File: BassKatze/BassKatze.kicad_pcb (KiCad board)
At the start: 2 copper layers, 16 parts, among them J1 USB_B_Micro, J2 Conn_01x02_Male, U1 ATmega328-AU, U2 MSGEQ7, U3 TP4056

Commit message: pcb wip
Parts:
- added Charge_Powerup1: D, Diode_THT:D_DO-15_P5.08mm_Vertical_KathodeUp, F.Cu at (73.0, 148.0)
- added D1: D, Diode_THT:D_DO-15_P2.54mm_Vertical_KathodeUp, F.Cu at (105.5, 112.9)
- added D10: SK6812, LED_SMD:LED_SK6812_PLCC4_5.0x5.0mm_P3.2mm, F.Cu at (116.8, 147.3)
- added D11: SK6812, LED_SMD:LED_SK6812_PLCC4_5.0x5.0mm_P3.2mm, F.Cu at (113.7, 141.0)
- added D12: SK6812, LED_SMD:LED_SK6812_PLCC4_5.0x5.0mm_P3.2mm, F.Cu at (111.8, 134.6)
- added D13: SK6812, LED_SMD:LED_SK6812_PLCC4_5.0x5.0mm_P3.2mm, F.Cu at (110.5, 128.3)
- added D14: SK6812, LED_SMD:LED_SK6812_PLCC4_5.0x5.0mm_P3.2mm, F.Cu at (110.5, 121.9)
- added D15: SK6812, LED_SMD:LED_SK6812_PLCC4_5.0x5.0mm_P3.2mm, F.Cu at (112.4, 115.6)
- added D16: SK6812, LED_SMD:LED_SK6812_PLCC4_5.0x5.0mm_P3.2mm, F.Cu at (113.7, 109.2)
- added D17: SK6812, LED_SMD:LED_SK6812_PLCC4_5.0x5.0mm_P3.2mm, F.Cu at (120.7, 106.0)
- added D2: SK6812, LED_SMD:LED_SK6812_PLCC4_5.0x5.0mm_P3.2mm, F.Cu at (137.2, 106.7)
- added D3: SK6812, LED_SMD:LED_SK6812_PLCC4_5.0x5.0mm_P3.2mm, F.Cu at (138.4, 113.7)
- added D4: SK6812, LED_SMD:LED_SK6812_PLCC4_5.0x5.0mm_P3.2mm, F.Cu at (144.8, 114.9)
- added D5: SK6812, LED_SMD:LED_SK6812_PLCC4_5.0x5.0mm_P3.2mm, F.Cu at (144.8, 121.9)
- added D6: SK6812, LED_SMD:LED_SK6812_PLCC4_5.0x5.0mm_P3.2mm, F.Cu at (144.8, 128.3)
- added D7: SK6812, LED_SMD:LED_SK6812_PLCC4_5.0x5.0mm_P3.2mm, F.Cu at (142.9, 134.6)
- added D8: SK6812, LED_SMD:LED_SK6812_PLCC4_5.0x5.0mm_P3.2mm, F.Cu at (140.3, 141.0)
- added D9: SK6812, LED_SMD:LED_SK6812_PLCC4_5.0x5.0mm_P3.2mm, F.Cu at (136.5, 147.3)
- added Q1: IRF7404, Package_SO:SOIC-8_3.9x4.9mm_P1.27mm, B.Cu at (146.8, 127.0)
- added R4: 250Ohm, Resistor_SMD:R_1206_3216Metric_Pad1.42x1.75mm_HandSolder, B.Cu at (141.6, 122.7)
- added R5: 10KOhm, Resistor_SMD:R_1206_3216Metric_Pad1.42x1.75mm_HandSolder, B.Cu at (137.2, 104.8)
- added SW1: SW_Push, Capacitor_SMD:C_1210_3225Metric, B.Cu at (145.7, 132.1)
- C1, C2, C3, C4, C5, C6, R1, R2, R3, RProg1, U1: moved to B.Cu
- J1: value USB_B_Micro -> Conn_01x02_Female; footprint Connector_PinHeader_2.54mm:PinHeader_1x06_P2.54mm_Vertical -> Capacitor_SMD:C_1210_3225Metric; moved to B.Cu
- J2: footprint Connector_JST:JST_EH_B2B-EH-A_1x02_P2.50mm_Vertical -> Capacitor_SMD:C_1210_3225Metric; moved to B.Cu
- U3: footprint Package_SO:HSOP-8-1EP_3.9x4.9mm_P1.27mm_EP2.41x3.1mm_ThermalVias -> tp4056:TP4056_SOP-8-PP; moved to B.Cu
- moved C4 93.0 mm to (119.1, 150.0), turned to 180 degrees
- moved U2 92.7 mm to (130.8, 149.9), turned to 180 degrees
- moved C6 90.5 mm to (119.3, 144.8), turned to 180 degrees
- moved R3 88.2 mm to (127.0, 152.9)
- moved C5 79.7 mm to (134.9, 149.9)
- moved C3 66.1 mm to (132.5, 139.4)
- moved R2 65.5 mm to (137.7, 139.4)
- moved J2 64.6 mm to (151.3, 133.2), turned to 90 degrees
- moved U3 57.4 mm to (145.3, 115.1)
- moved J1 56.5 mm to (127.1, 113.9)
- moved U1 56.4 mm to (116.8, 110.5)
- moved R1 53.2 mm to (132.5, 114.0)
- moved C2 53.0 mm to (151.5, 121.4), turned to 90 degrees
- moved C1 46.0 mm to (145.3, 119.5), turned to 180 degrees
- moved RProg1 45.0 mm to (138.6, 116.8), turned to 270 degrees
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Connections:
- ISP1 pad 2: SCK -> (no net)
- ISP1 pad 3: Reset -> SCK
- ISP1 pad 4: BAT- -> MOSI
- ISP1 pad 5: MOSI -> Reset
- ISP1 pad 6: (no net) -> BAT-
- J1 pad 1: 5V_IN -> BAT-
- J1 pad 2: (no net) -> 5V_IN
- U1 pad 11: (no net) -> STDBY
- U1 pad 2: (no net) -> Button
- U1 pad 32: (no net) -> LED1
- U1 pad 9: (no net) -> PWR_HOLD
- U3 pad 6: (no net) -> STDBY
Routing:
- net BAT-: track 0.00 -> 263.0 mm, vias 0 -> 8
- net PWR: track 0.00 -> 169.2 mm, vias 0 -> 4
- net RAW_Spectrum: track 0.00 -> 51.2 mm, vias 0 -> 3
- net EQ_Band: track 0.00 -> 44.3 mm
- net EQ_Reset: track 0.00 -> 44.1 mm
- net LED1: track 0.00 -> 30.0 mm, vias 0 -> 3
- net Reset: track 0.00 -> 29.1 mm
- net Net-(D10-Pad2): track 0.00 -> 25.1 mm
- net BAT+: track 0.00 -> 24.2 mm
- net MOSI: track 0.00 -> 13.8 mm
- net Net-(C1-Pad1): track 0.00 -> 12.0 mm
- net Net-(D10-Pad4): track 0.00 -> 9.39 mm
- net Net-(D11-Pad4): track 0.00 -> 8.38 mm
- net Button: track 0.00 -> 8.28 mm
- net SCK: track 0.00 -> 8.12 mm
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
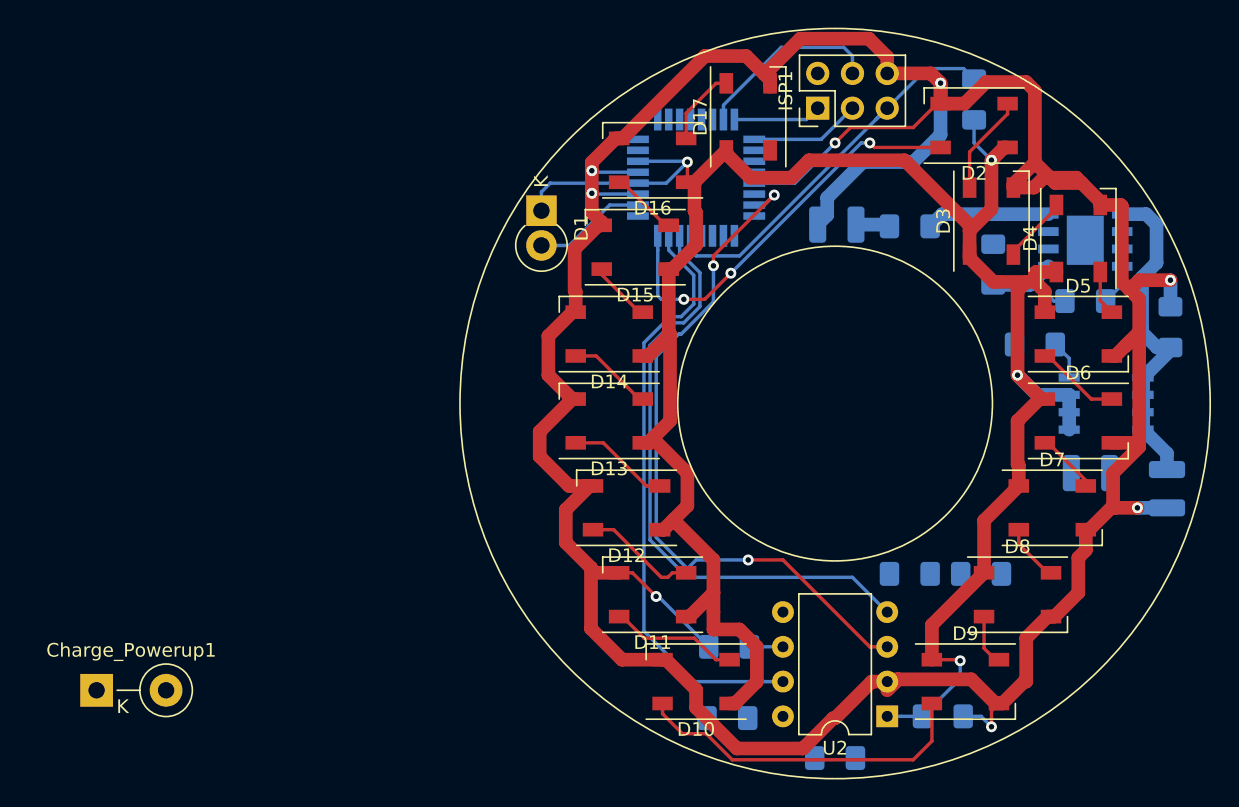
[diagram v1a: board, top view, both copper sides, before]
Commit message: with mic amplifier
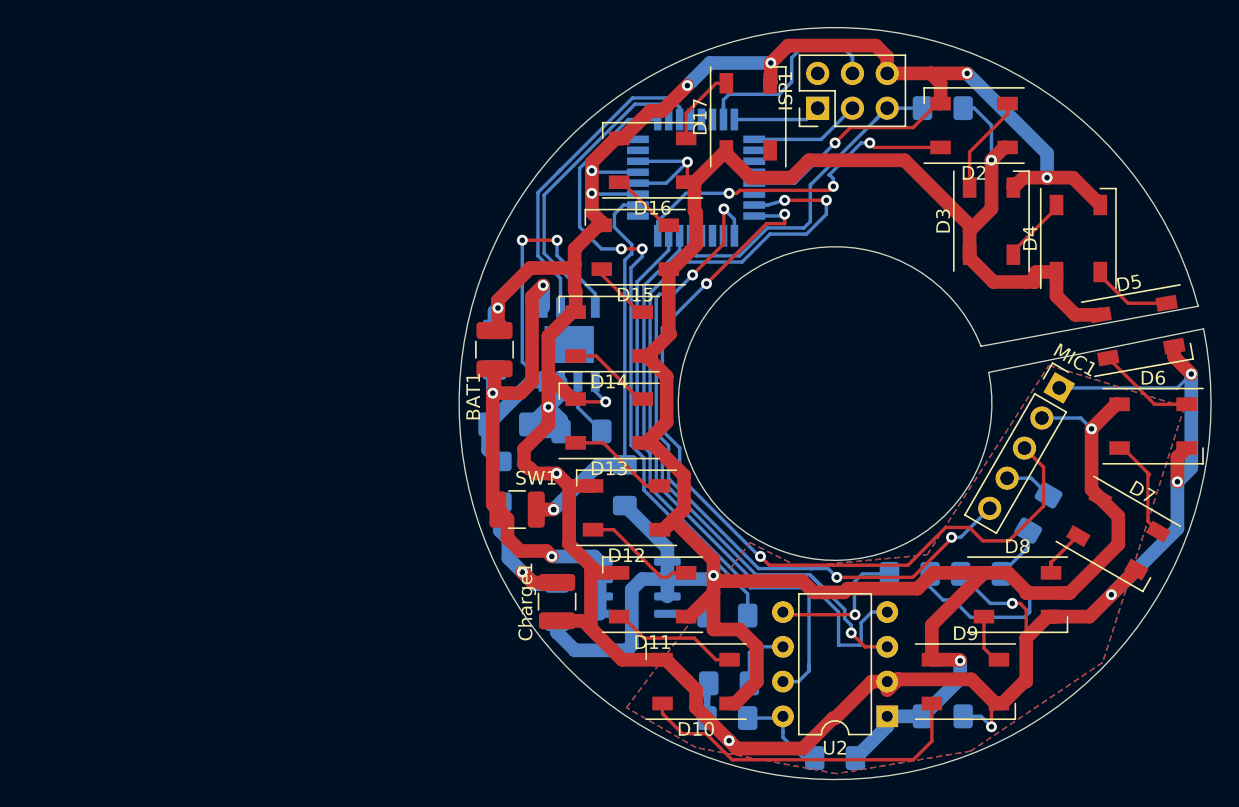
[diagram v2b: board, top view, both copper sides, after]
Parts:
- removed J1: Conn_01x02_Female, Capacitor_SMD:C_1210_3225Metric
- removed J2: Conn_01x02_Male, Capacitor_SMD:C_1210_3225Metric
- added BAT1: BAT, Capacitor_SMD:C_1210_3225Metric, F.Cu at (102.1, 123.1)
- added Charge1: Charge, Capacitor_SMD:C_1210_3225Metric, F.Cu at (106.7, 141.5)
- added MIC1: MIC, Connector_PinHeader_2.54mm:PinHeader_1x05_P2.54mm_Vertical, F.Cu at (143.4, 125.9)
- added R6: 147KOhm, Resistor_SMD:R_1206_3216Metric_Pad1.42x1.75mm_HandSolder, B.Cu at (141.9, 135.0)
- Charge_Powerup1: footprint Diode_THT:D_DO-15_P5.08mm_Vertical_KathodeUp -> Diode_SMD:D_1206_3216Metric; moved to B.Cu
- D1: footprint Diode_THT:D_DO-15_P2.54mm_Vertical_KathodeUp -> Diode_SMD:D_1206_3216Metric_Pad1.42x1.75mm_HandSolder; moved to B.Cu
- R2: value 22KOhm -> 26KOhm
- SW1: moved to F.Cu
- moved C2 49.4 mm to (102.1, 123.1)
- moved C1 43.1 mm to (103.1, 128.5), turned to 0 degrees
- moved SW1 42.0 mm to (103.8, 134.7), turned to 0 degrees
- moved U3 38.5 mm to (107.6, 122.7), turned to 90 degrees
- moved Q1 37.1 mm to (112.3, 140.5), turned to 180 degrees
- moved R1 35.3 mm to (102.5, 132.7), turned to 90 degrees
- moved Charge_Powerup1 34.2 mm to (106.7, 141.6), turned to 90 degrees
- moved RProg1 32.5 mm to (108.5, 129.0), turned to 180 degrees
- moved R4 30.0 mm to (119.1, 142.5), turned to 0 degrees
- moved D1 21.0 mm to (111.6, 133.0), turned to 90 degrees
- moved D6 5.47 mm to (150.2, 128.7)
- moved D7 5.19 mm to (147.7, 136.5), turned to 330 degrees
- moved D5 4.33 mm to (149.1, 121.7), turned to 10 degrees
- moved C6 2.67 mm to (119.3, 147.4)
- moved R5 2.37 mm to (134.9, 105.4), turned to 0 degrees
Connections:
- R2 pad 1: Net-(C3-Pad2) -> BAT-
- R2 pad 2: (no net) -> Net-(C3-Pad2)
- U1 pad 10: (no net) -> CHRG
- U1 pad 24: (no net) -> Gain_Select
- U1 pad 25: (no net) -> Attack_Select
- U3 pad 7: (no net) -> CHRG
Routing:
- net Gain_Select: track 0.00 -> 63.2 mm, vias 0 -> 3
- net Attack_Select: track 0.00 -> 53.7 mm, vias 0 -> 4
- net PWR_HOLD: track 0.00 -> 47.4 mm, vias 0 -> 2
- net PWR: track 169.2 -> 213.5 mm, vias 4 -> 5
- net STDBY: track 0.00 -> 23.8 mm
- net CHRG: track 0.00 -> 22.2 mm
- net Button: track 8.28 -> 30.4 mm, vias 0 -> 2
- net Net-(C3-Pad2): track 0.00 -> 17.7 mm
- net Net-(C1-Pad1): track 12.0 -> 28.4 mm, vias 0 -> 2
- net BAT+: track 24.2 -> 38.1 mm, vias 0 -> 3
- net Net-(C3-Pad1): track 0.00 -> 10.6 mm, vias 0 -> 1
- net RAW_Spectrum: track 51.2 -> 61.7 mm
- net 5V_IN: track 2.50 -> 11.6 mm, vias 0 -> 1
- net Net-(C4-Pad1): track 0.00 -> 7.12 mm
- net LED1: track 30.0 -> 25.2 mm
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- added copper zone on B.Cu, net BAT-
- added copper zone on F.Cu, net BAT-
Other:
- board outline added: 55 x 54.9 mm

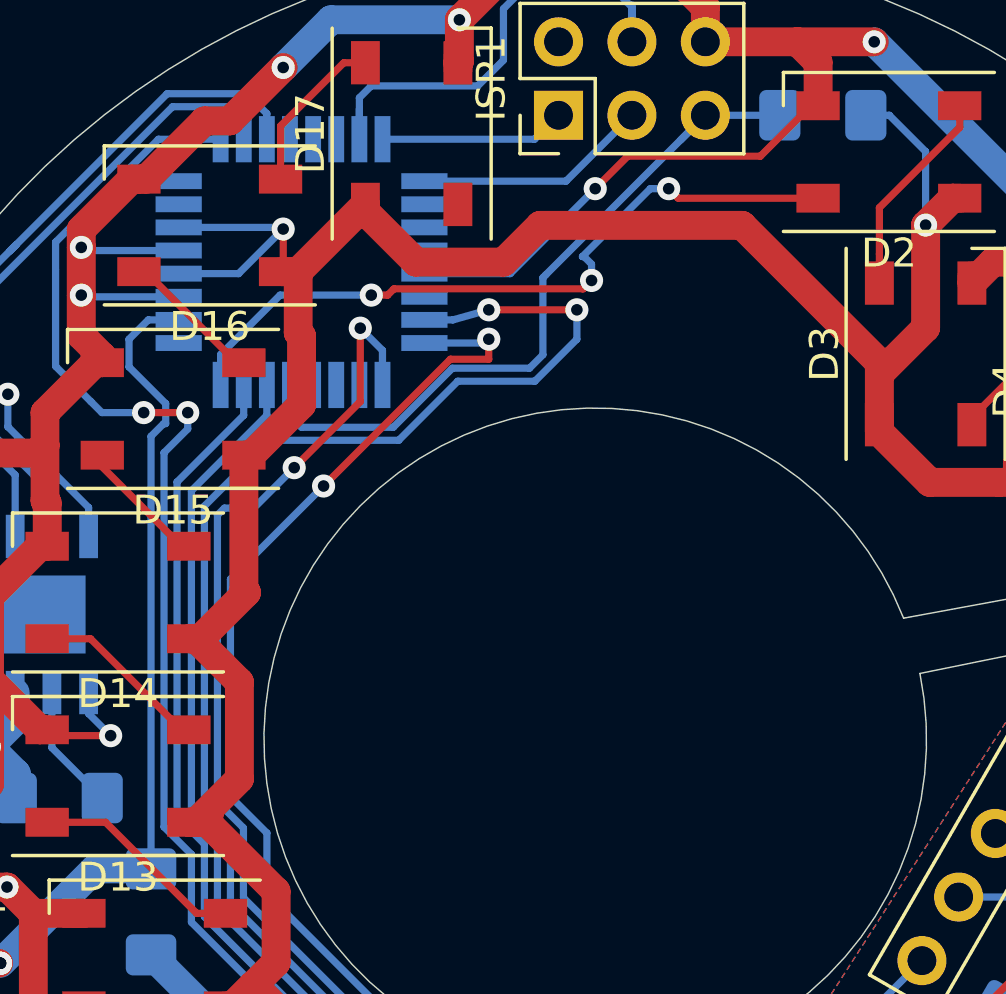
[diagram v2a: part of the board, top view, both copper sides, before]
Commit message: added rx/tx header for serial debugging started dummy application
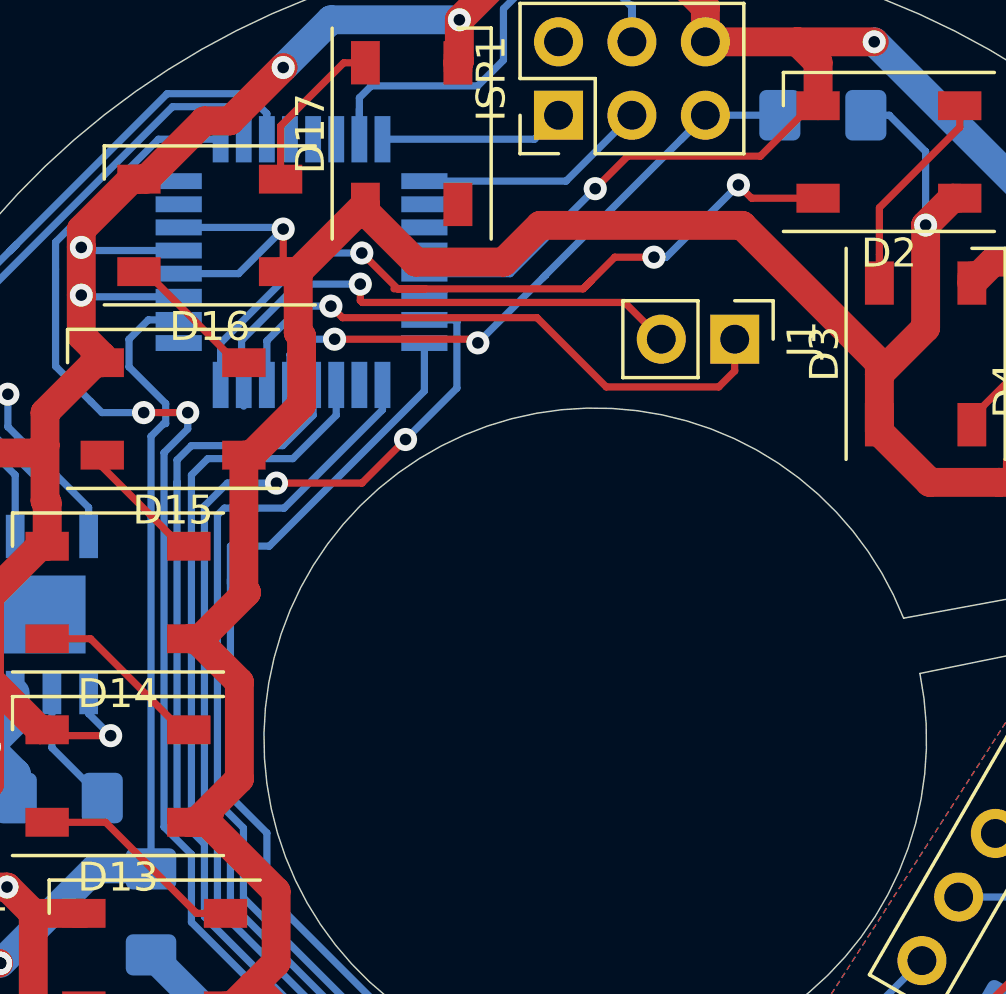
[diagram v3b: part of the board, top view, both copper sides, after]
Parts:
- added J1: Conn_01x02_Female, Connector_PinHeader_2.54mm:PinHeader_1x02_P2.54mm_Vertical, F.Cu at (131.8, 113.2)
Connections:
- U1 pad 27: (no net) -> EQ_Band
- U1 pad 28: (no net) -> EQ_Reset
- U1 pad 30: EQ_Band -> Net-(J1-Pad1)
- U1 pad 31: EQ_Reset -> Net-(J1-Pad2)
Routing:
- net Net-(J1-Pad1): track 0.00 -> 20.7 mm, vias 0 -> 1
- net Net-(J1-Pad2): track 0.00 -> 18.8 mm, vias 0 -> 1
- net RAW_Spectrum: track 61.7 -> 54.0 mm
- net Attack_Select: track 53.7 -> 50.5 mm, vias 4 -> 2
- net Gain_Select: track 63.2 -> 60.0 mm, vias 3 -> 1
- net LED1: track 25.2 -> 28.0 mm
- net EQ_Band: track 44.7 -> 47.4 mm
- net Reset: track 25.4 -> 22.9 mm, vias 0 -> 2
- net EQ_Reset: track 43.5 -> 45.8 mm

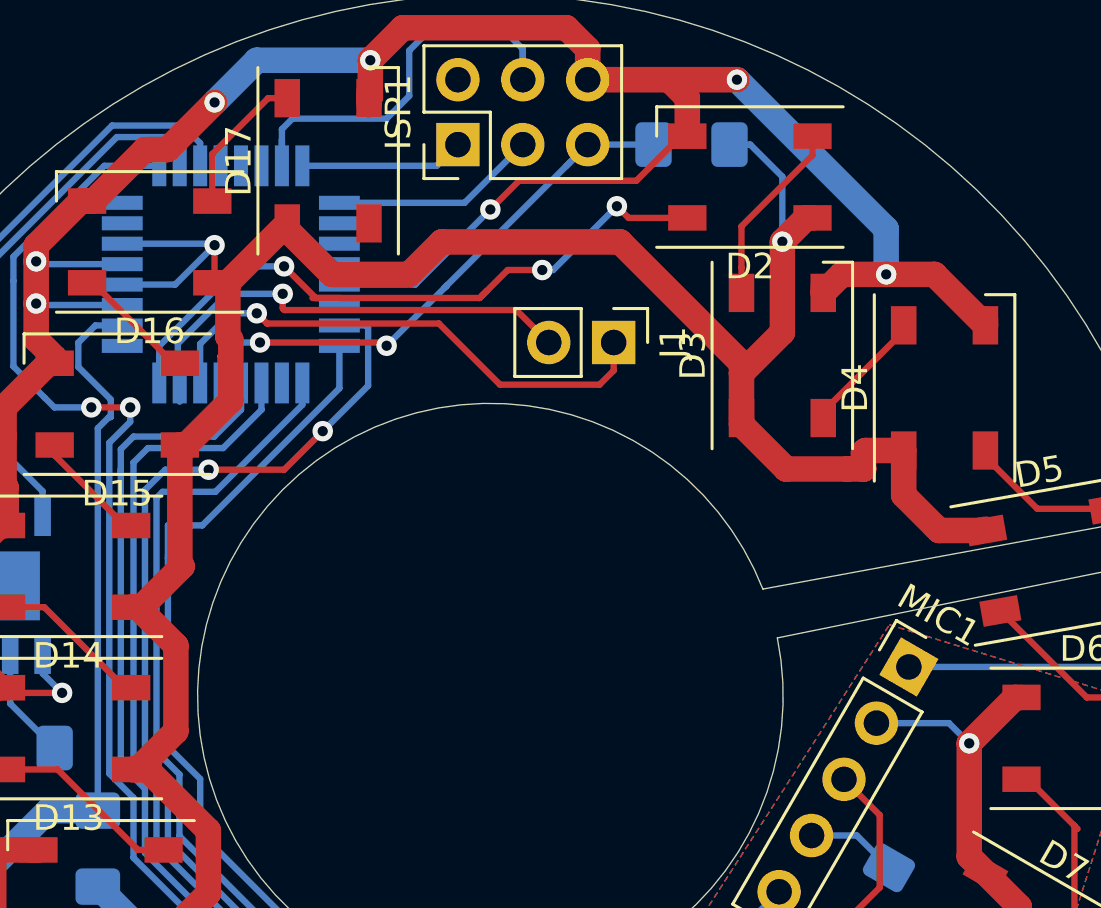
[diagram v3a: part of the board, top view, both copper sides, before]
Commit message: added voltage measure prescaler
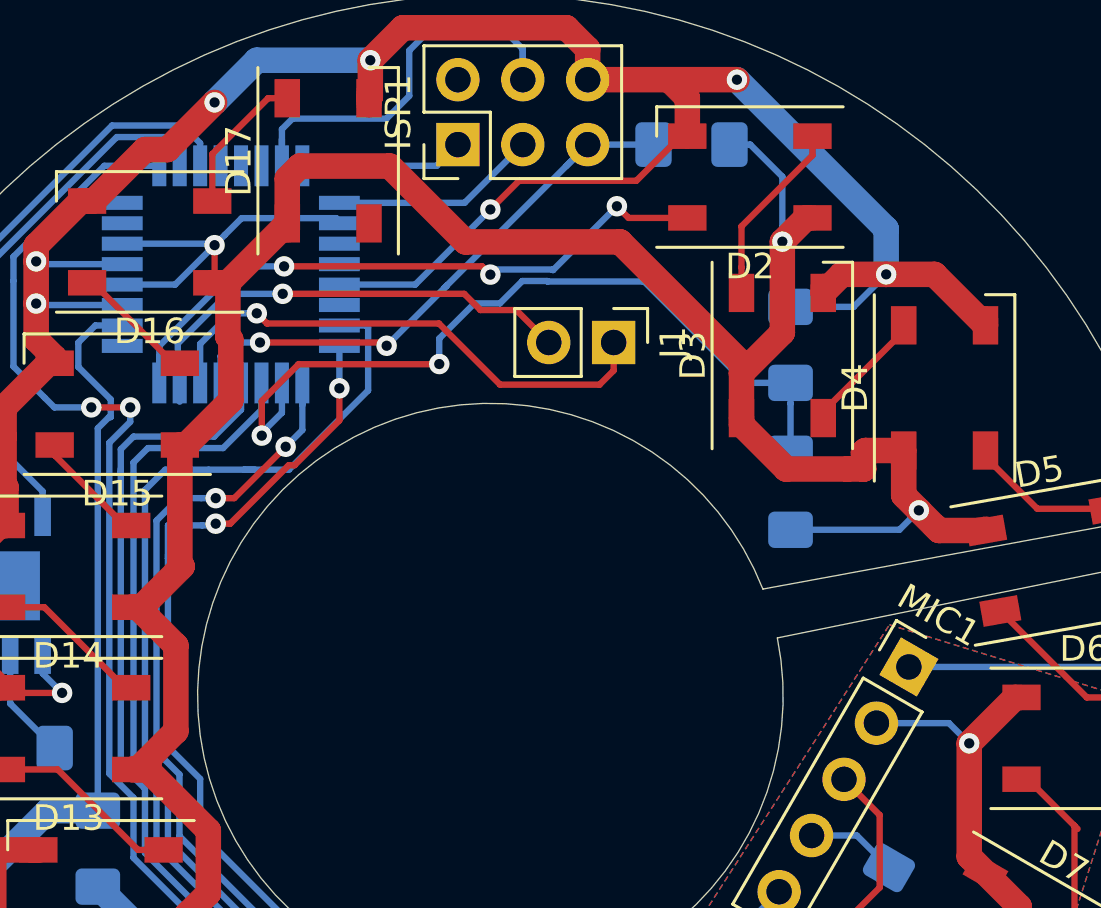
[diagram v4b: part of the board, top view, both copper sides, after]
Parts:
- added R7: 1KOhm, Resistor_SMD:R_1206_3216Metric_Pad1.42x1.75mm_HandSolder, B.Cu at (138.8, 113.2)
- added R8: 5KOhm, Resistor_SMD:R_1206_3216Metric_Pad1.42x1.75mm_HandSolder, B.Cu at (138.8, 119.0)
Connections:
- U1 pad 18: (no net) -> PWR
- U1 pad 26: (no net) -> Net-(R7-Pad1)
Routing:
- net Net-(R7-Pad1): track 0.00 -> 31.4 mm, vias 0 -> 2
- net PWR: track 213.5 -> 226.2 mm, vias 5 -> 6
- net BAT-: track 259.1 -> 263.4 mm
- net LED1: track 28.0 -> 25.9 mm
- net Attack_Select: track 50.5 -> 51.3 mm, vias 2 -> 4
- net Gain_Select: track 60.0 -> 60.7 mm, vias 1 -> 3
- net RAW_Spectrum: track 54.0 -> 54.5 mm, vias 3 -> 1
